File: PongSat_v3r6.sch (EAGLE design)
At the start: 33 parts, among them U1 MIC5129 3v3, U2 Micro SD, X1 USB-MICROB, Y1 8MHz

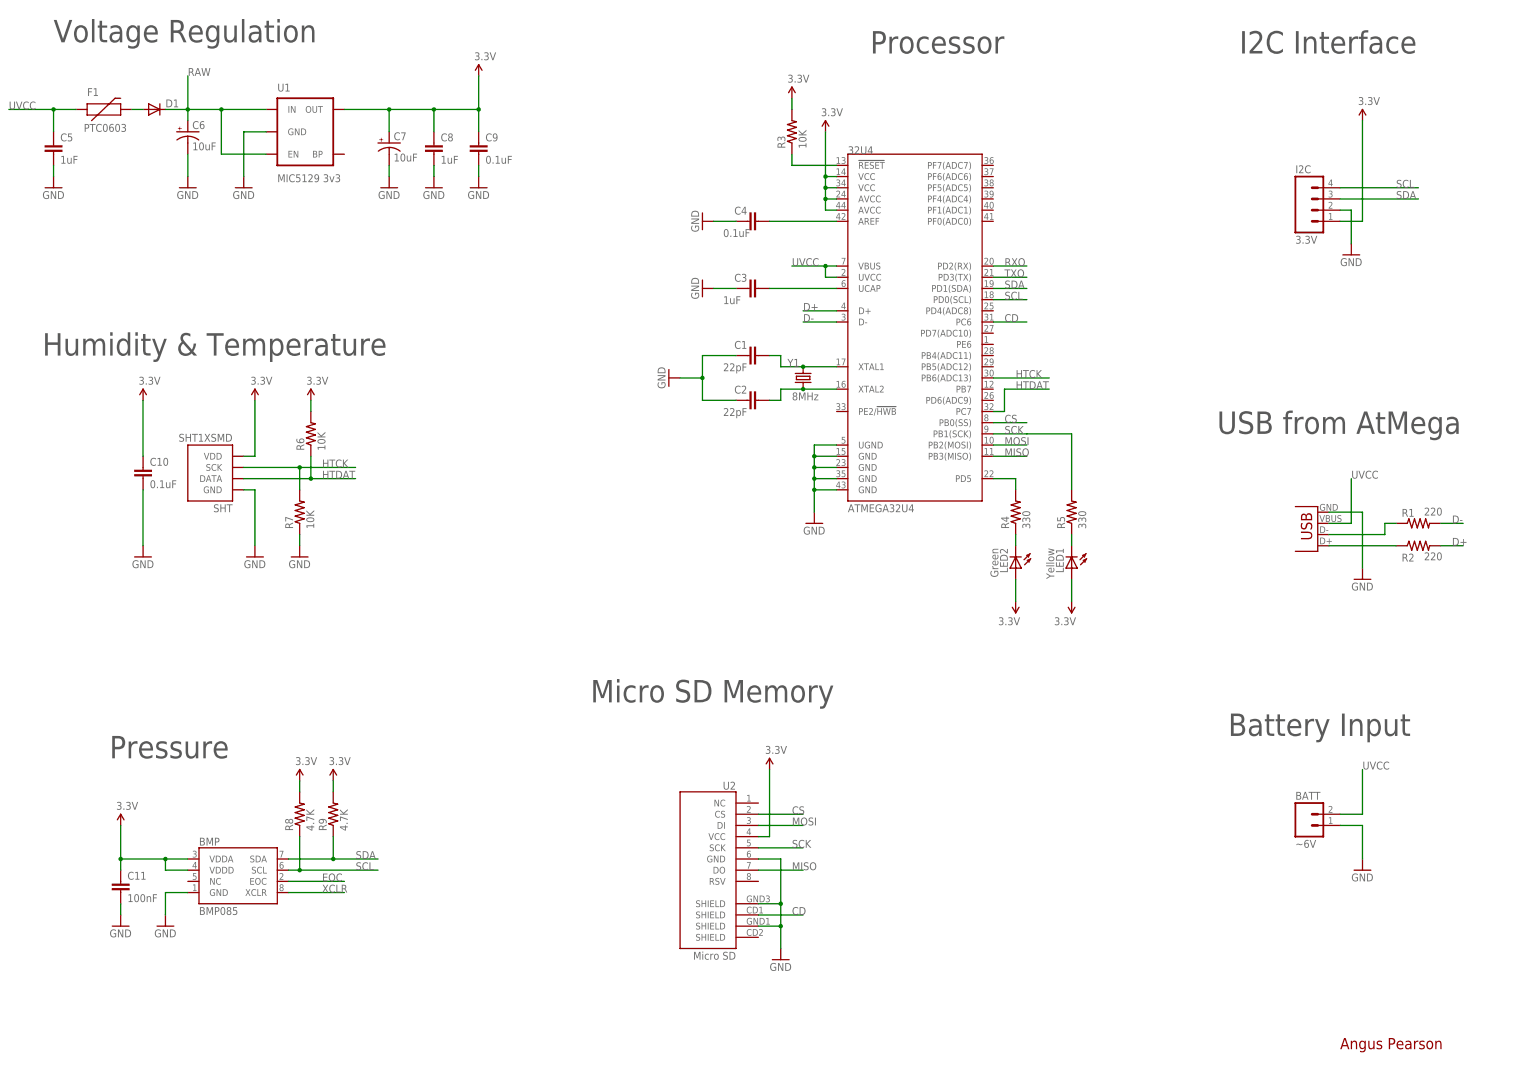
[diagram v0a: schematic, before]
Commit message: Revision 6
Removed acid traps and improved silkscreen. New rev 6 gerber files as
well. Version 4 will be along soon in the main branch…
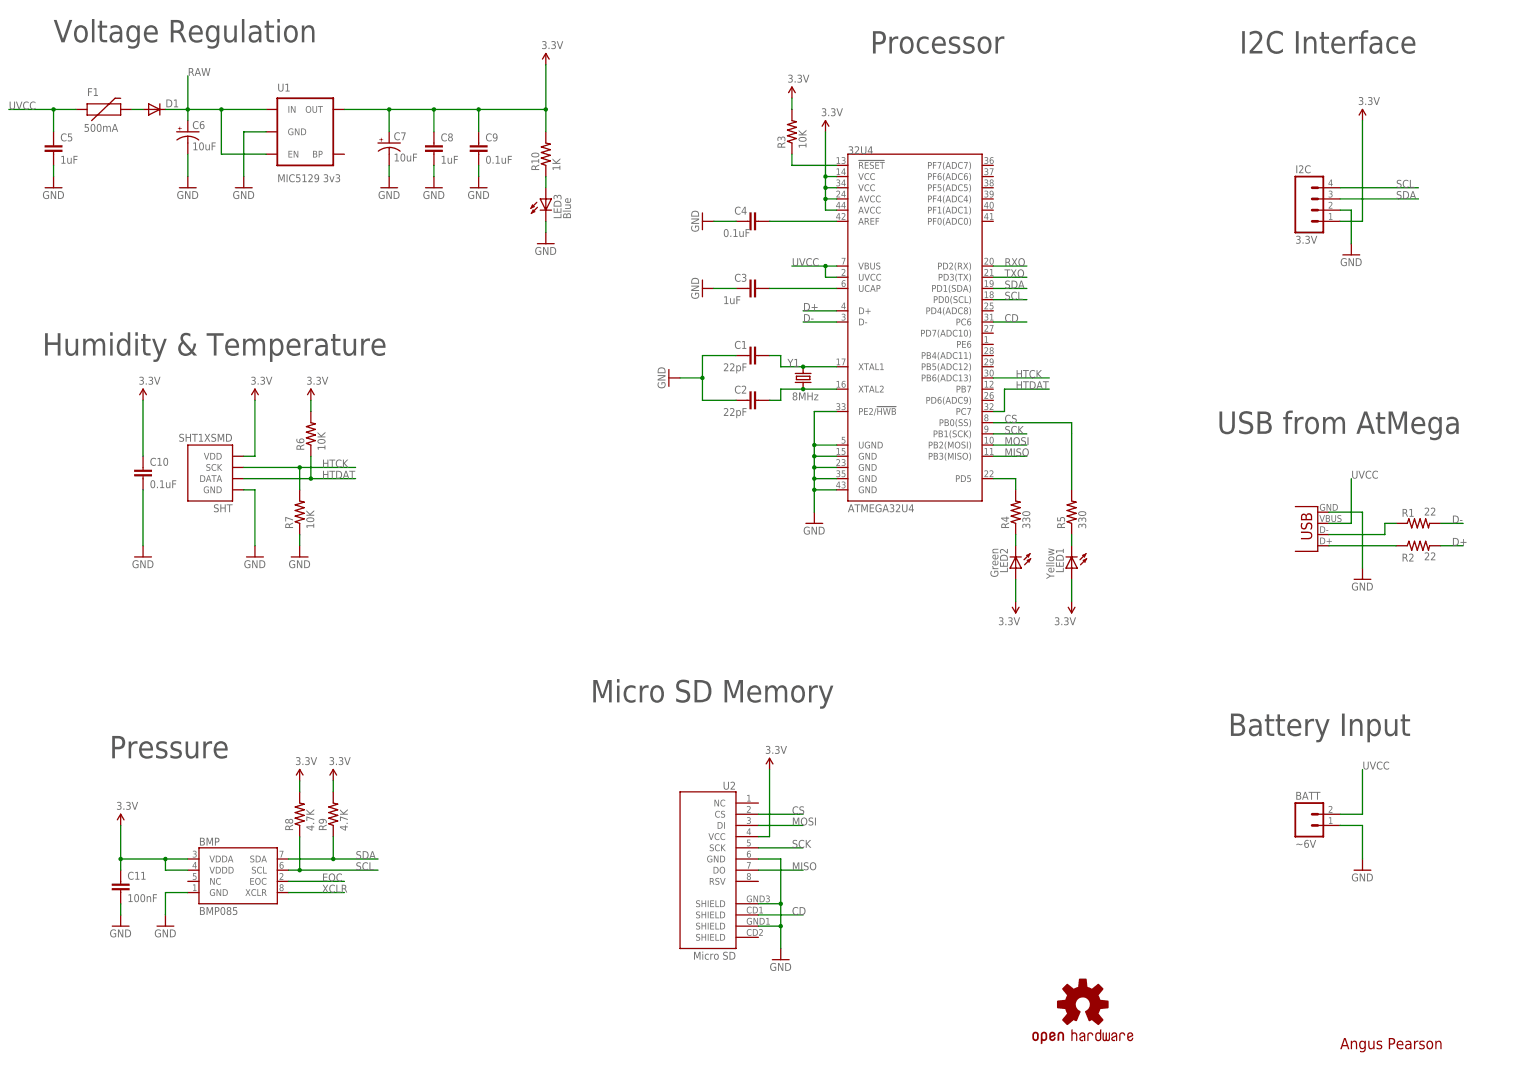
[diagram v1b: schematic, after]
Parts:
- added LED3: Blue, SparkFun-LED:LED0603
- added R10: 1K, SparkFun-Passives:RESISTOR0402-RES
- added U$2: OSHW-LOGOS, SparkFun-Aesthetics:OSHW-LOGOS
- F1: value PTC0603 -> 500mA
- R1, R2: value 220 -> 22
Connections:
- new net N$8: LED3.A, R10.1
- net 3.3V: now also R10.2
- net CS: now also R5.2
- net GND: now also 32U4.PE2/!HWB, LED3.C
- net SCK: no longer R5.2
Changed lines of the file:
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@@
 <part name="X1" library="SparkFun-Connectors" deviceset="USB" device="-MICROB"/>
 <part name="GND3" library="SparkFun-Aesthetics" deviceset="GND" device=""/>
-<part name="R1" library="SparkFun-Passives" deviceset="RESISTOR" device="0402-RES" value="220"/>
-<part name="R2" library="SparkFun-Passives" deviceset="RESISTOR" device="0402-RES" value="220"/>
+<part name="R1" library="SparkFun-Passives" deviceset="RESISTOR" device="0402-RES" value="22"/>
+<part name="R2" library="SparkFun-Passives" deviceset="RESISTOR" device="0402-RES" value="22"/>
 <part name="C3" library="SparkFun-Passives" deviceset="CAP" device="0402-CAP" value="1uF"/>
 <part name="GND4" library="SparkFun-Aesthetics" deviceset="GND" device=""/>
@@
 <part name="GND6" library="SparkFun-Aesthetics" deviceset="GND" device=""/>
 <part name="U1" library="SparkFun-PowerIC" deviceset="V_REG_MIC5219" device="SMD" value="MIC5129 3v3"/>
-<part name="P+2" library="SparkFun-Aesthetics" deviceset="3.3V" device=""/>
 <part name="GND7" library="SparkFun-Aesthetics" deviceset="GND" device=""/>
 <part name="C6" library="SparkFun-Passives" deviceset="CAP_POL" device="1206-KIT" value="10uF"/>
 <part name="GND8" library="SparkFun-Aesthetics" deviceset="GND" device=""/>
 <part name="D1" library="SparkFun-DiscreteSemi" deviceset="DIODE" device="SOT23"/>
-<part name="F1" library="SparkFun-PowerIC" deviceset="PTC" device="0603"/>
+<part name="F1" library="SparkFun-PowerIC" deviceset="PTC" device="0603" value="500mA"/>
 <part name="C7" library="SparkFun-Passives" deviceset="CAP_POL" device="1206-KIT" value="10uF"/>
 <part name="C8" library="SparkFun-Passives" deviceset="CAP" device="0402-CAP" value="1uF"/>
@@
 <part name="BATT" library="SparkFun-Connectors" deviceset="M02" device="PTH" value="~6V"/>
 <part name="GND19" library="SparkFun-Aesthetics" deviceset="GND" device=""/>
+<part name="LED3" library="SparkFun-LED" deviceset="LED" device="0603" value="Blue"/>
+<part name="R10" library="SparkFun-Passives" deviceset="RESISTOR" device="0402-RES" value="1K"/>
+<part name="GND20" library="SparkFun-Aesthetics" deviceset="GND" device=""/>
+<part name="P+2" library="SparkFun-Aesthetics" deviceset="3.3V" device=""/>
+<part name="U$2" library="SparkFun-Aesthetics" deviceset="OSHW-LOGO" device="S"/>
 </parts>
 <sheets>
@@
 <instance part="GND6" gate="1" x="40.64" y="200.66"/>
 <instance part="U1" gate="G$1" x="99.06" y="213.36"/>
-<instance part="P+2" gate="G$1" x="137.16" y="226.06"/>
 <instance part="GND7" gate="1" x="83.82" y="200.66"/>
 <instance part="C6" gate="G$1" x="71.12" y="213.36"/>
@@
 <instance part="BATT" gate="G$1" x="325.12" y="55.88"/>
 <instance part="GND19" gate="1" x="337.82" y="45.72"/>
+<instance part="LED3" gate="G$1" x="152.4" y="198.12"/>
+<instance part="R10" gate="G$1" x="152.4" y="208.28" rot="R90"/>
+<instance part="GND20" gate="1" x="152.4" y="187.96"/>
+<instance part="P+2" gate="G$1" x="152.4" y="228.6"/>
+<instance part="U$2" gate="G$1" x="274.32" y="15.24"/>
 </instances>
 <busses>
@@
 <junction x="213.36" y="134.62"/>
 <junction x="213.36" y="132.08"/>
+<pinref part="32U4" gate="G$1" pin="PE2/!HWB"/>
+<wire x1="218.44" y1="149.86" x2="213.36" y2="149.86" width="0.1524" layer="91"/>
+<wire x1="213.36" y1="149.86" x2="213.36" y2="142.24" width="0.1524" layer="91"/>
+<junction x="213.36" y="142.24"/>
 </segment>
 <segment>
@@
 <pinref part="GND19" gate="1" pin="GND"/>
 </segment>
+<segment>
+<pinref part="LED3" gate="G$1" pin="C"/>
+<pinref part="GND20" gate="1" pin="GND"/>
+<wire x1="152.4" y1="193.04" x2="152.4" y2="190.5" width="0.1524" layer="91"/>
+</segment>
 </net>
 <net name="N$3" class="0">
@@
 <net name="SCK" class="0">
 <segment>
+<pinref part="U2" gate="G$1" pin="SCK"/>
+<wire x1="200.66" y1="50.8" x2="210.82" y2="50.8" width="0.2032" layer="91"/>
+<label x="208.28" y="50.8" size="1.778" layer="95"/>
+</segment>
+<segment>
 <pinref part="32U4" gate="G$1" pin="PB1(SCK)"/>
 <wire x1="254" y1="144.78" x2="261.62" y2="144.78" width="0.1524" layer="91"/>
 <label x="256.54" y="144.78" size="1.778" layer="95"/>
-<pinref part="R5" gate="G$1" pin="2"/>
-<wire x1="271.78" y1="132.08" x2="271.78" y2="144.78" width="0.2032" layer="91"/>
-<wire x1="271.78" y1="144.78" x2="261.62" y2="144.78" width="0.2032" layer="91"/>
-</segment>
-<segment>
-<pinref part="U2" gate="G$1" pin="SCK"/>
-<wire x1="200.66" y1="50.8" x2="210.82" y2="50.8" width="0.2032" layer="91"/>
-<label x="208.28" y="50.8" size="1.778" layer="95"/>
 </segment>
 </net>
@@
 <pinref part="R3" gate="G$1" pin="2"/>
 <wire x1="208.28" y1="220.98" x2="208.28" y2="218.44" width="0.2032" layer="91"/>
-</segment>
-<segment>
-<pinref part="P+2" gate="G$1" pin="3.3V"/>
-<wire x1="137.16" y1="226.06" x2="137.16" y2="218.44" width="0.1524" layer="91"/>
-<pinref part="U1" gate="G$1" pin="OUT"/>
-<pinref part="C9" gate="G$1" pin="1"/>
-<wire x1="137.16" y1="218.44" x2="127" y2="218.44" width="0.1524" layer="91"/>
-<wire x1="127" y1="218.44" x2="116.84" y2="218.44" width="0.1524" layer="91"/>
-<wire x1="116.84" y1="218.44" x2="106.68" y2="218.44" width="0.1524" layer="91"/>
-<wire x1="137.16" y1="213.36" x2="137.16" y2="218.44" width="0.2032" layer="91"/>
-<pinref part="C8" gate="G$1" pin="1"/>
-<wire x1="127" y1="213.36" x2="127" y2="218.44" width="0.2032" layer="91"/>
-<pinref part="C7" gate="G$1" pin="+"/>
-<wire x1="116.84" y1="213.36" x2="116.84" y2="218.44" width="0.2032" layer="91"/>
-<junction x="116.84" y="218.44"/>
-<junction x="127" y="218.44"/>
-<junction x="137.16" y="218.44"/>
 </segment>
 <segment>
@@
 <wire x1="104.14" y1="66.04" x2="104.14" y2="63.5" width="0.2032" layer="91"/>
 </segment>
+<segment>
+<pinref part="U1" gate="G$1" pin="OUT"/>
+<pinref part="C9" gate="G$1" pin="1"/>
+<wire x1="137.16" y1="218.44" x2="127" y2="218.44" width="0.1524" layer="91"/>
+<wire x1="127" y1="218.44" x2="116.84" y2="218.44" width="0.1524" layer="91"/>
+<wire x1="116.84" y1="218.44" x2="106.68" y2="218.44" width="0.1524" layer="91"/>
+<wire x1="137.16" y1="213.36" x2="137.16" y2="218.44" width="0.2032" layer="91"/>
+<pinref part="C8" gate="G$1" pin="1"/>
+<wire x1="127" y1="213.36" x2="127" y2="218.44" width="0.2032" layer="91"/>
+<pinref part="C7" gate="G$1" pin="+"/>
+<wire x1="116.84" y1="213.36" x2="116.84" y2="218.44" width="0.2032" layer="91"/>
+<junction x="116.84" y="218.44"/>
+<junction x="127" y="218.44"/>
+<junction x="137.16" y="218.44"/>
+<pinref part="R10" gate="G$1" pin="2"/>
+<wire x1="152.4" y1="213.36" x2="152.4" y2="218.44" width="0.1524" layer="91"/>
+<wire x1="152.4" y1="218.44" x2="137.16" y2="218.44" width="0.1524" layer="91"/>
+<pinref part="P+2" gate="G$1" pin="3.3V"/>
+<wire x1="152.4" y1="228.6" x2="152.4" y2="218.44" width="0.1524" layer="91"/>
+<junction x="152.4" y="218.44"/>
+</segment>
 </net>
 <net name="CS" class="0">
 <segment>
 <pinref part="32U4" gate="G$1" pin="PB0(SS)"/>
-<wire x1="254" y1="147.32" x2="261.62" y2="147.32" width="0.1524" layer="91"/>
 <label x="256.54" y="147.32" size="1.778" layer="95"/>
+<pinref part="R5" gate="G$1" pin="2"/>
+<wire x1="271.78" y1="132.08" x2="271.78" y2="144.78" width="0.2032" layer="91"/>
+<wire x1="254" y1="147.32" x2="271.78" y2="147.32" width="0.1524" layer="91"/>
+<wire x1="271.78" y1="147.32" x2="271.78" y2="144.78" width="0.1524" layer="91"/>
 </segment>
 <segment>
@@
 </segment>
 </net>
+<net name="N$8" class="0">
+<segment>
+<pinref part="R10" gate="G$1" pin="1"/>
+<pinref part="LED3" gate="G$1" pin="A"/>
+<wire x1="152.4" y1="203.2" x2="152.4" y2="200.66" width="0.1524" layer="91"/>
+</segment>
+</net>

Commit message: Minor Fixes
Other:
- note added: "DIO 10"
- note added: "DIO 13"
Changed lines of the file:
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@@
 <text x="304.8" y="144.78" size="5.08" layer="97">USB from AtMega</text>
 <text x="307.34" y="76.2" size="5.08" layer="97">Battery Input</text>
+<text x="269.24" y="157.48" size="1.778" layer="97">DIO 10</text>
+<text x="269.24" y="154.94" size="1.778" layer="97">DIO 13</text>
 </plain>
 <instances>
